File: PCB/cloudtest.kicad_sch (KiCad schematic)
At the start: 10 parts, among them J1 PulseIn, J2 Display, U1 ESP32-C3_SUPERMINI_TH, U2 MIC5219-5.0YM5, U3 MIC5219-3.3YM5

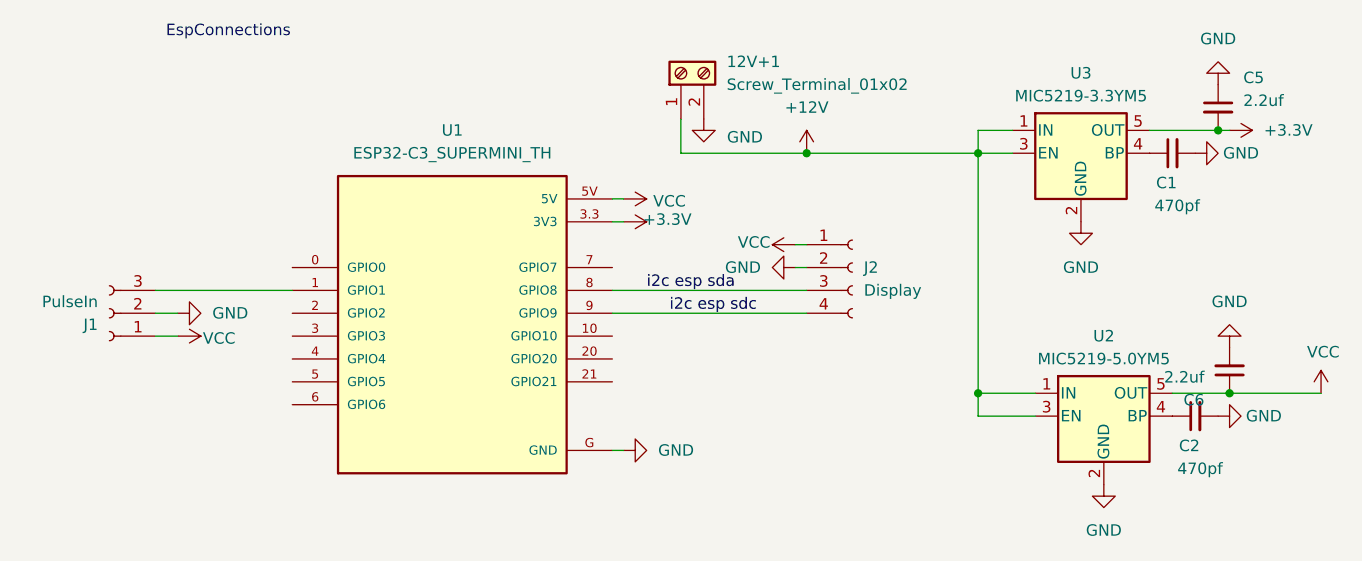
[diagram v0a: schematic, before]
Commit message: PCB update, remove power delivery
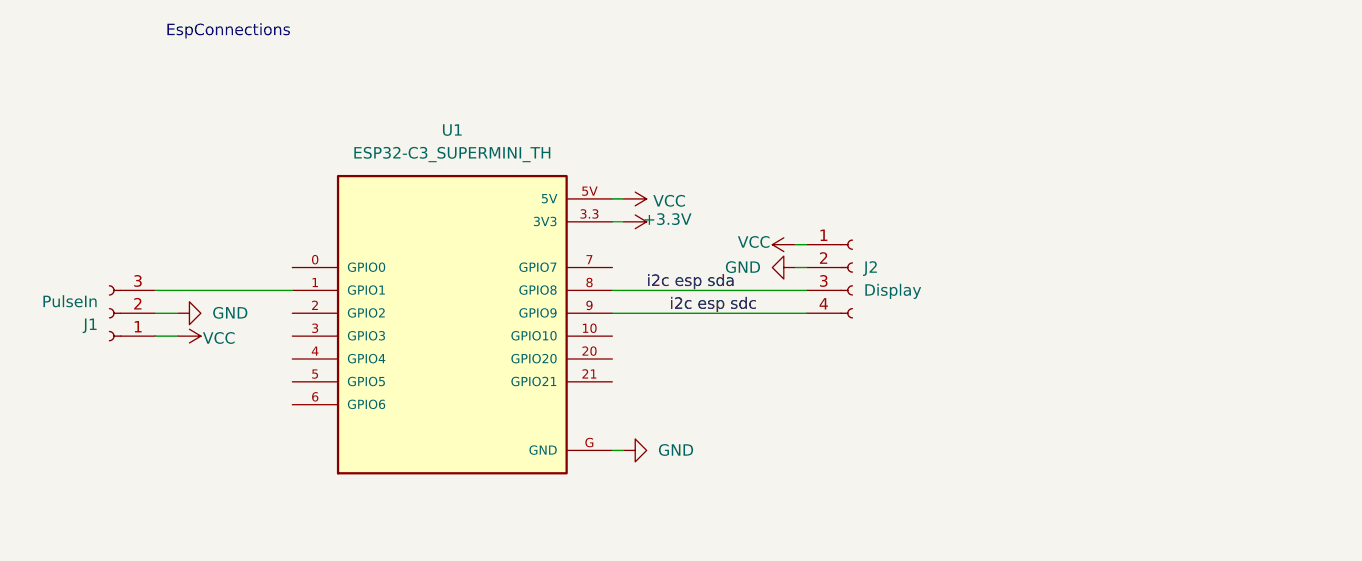
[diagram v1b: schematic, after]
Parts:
- removed 12V+1: Screw_Terminal_01x02, TerminalBlock:TerminalBlock_bornier-2_P5.08mm, symbol Connector:Screw_Terminal_01x02
- removed C1, C2: 470pf, Capacitor_THT:C_Disc_D5.0mm_W2.5mm_P5.00mm, symbol Device:C_Small
- removed C5, C6: 2.2uf, Capacitor_THT:CP_Radial_D5.0mm_P2.50mm, symbol Device:C_Small
- removed U2: MIC5219-5.0YM5, Package_TO_SOT_SMD:SOT-23-5, symbol Regulator_Linear:MIC5219-5.0YM5
- removed U3: MIC5219-3.3YM5, Package_TO_SOT_SMD:SOT-23-5, symbol Regulator_Linear:MIC5219-3.3YM5
- J1: footprint Connector_PinHeader_1.27mm:PinHeader_1x03_P1.27mm_Vertical -> Connector_PinHeader_2.54mm:PinHeader_1x03_P2.54mm_Vertical
- J2: footprint Connector_PinHeader_1.27mm:PinHeader_1x04_P1.27mm_Vertical -> Connector_PinHeader_2.54mm:PinHeader_1x04_P2.54mm_Vertical
